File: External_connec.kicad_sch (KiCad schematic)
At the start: 8 parts, among them J2 A - B, J3 H - L, J4 TYPE-C-31-M12_13, J5 EXT_LOAD, J6 R4_TX, J7 R4_RX

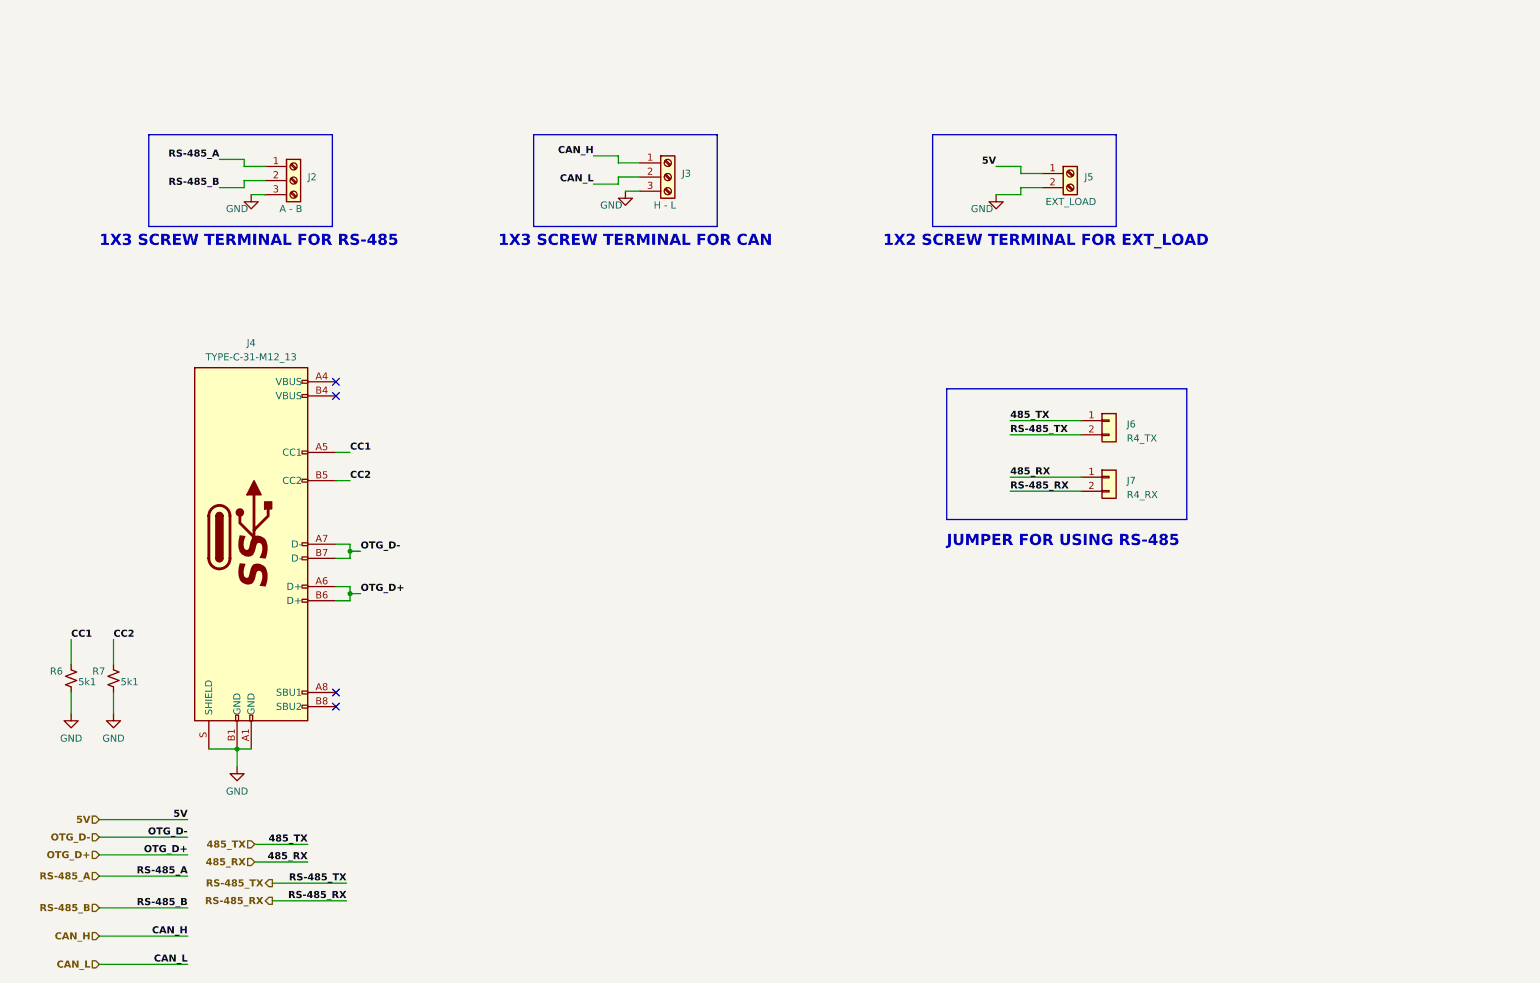
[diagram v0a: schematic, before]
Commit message: Added Female Headers
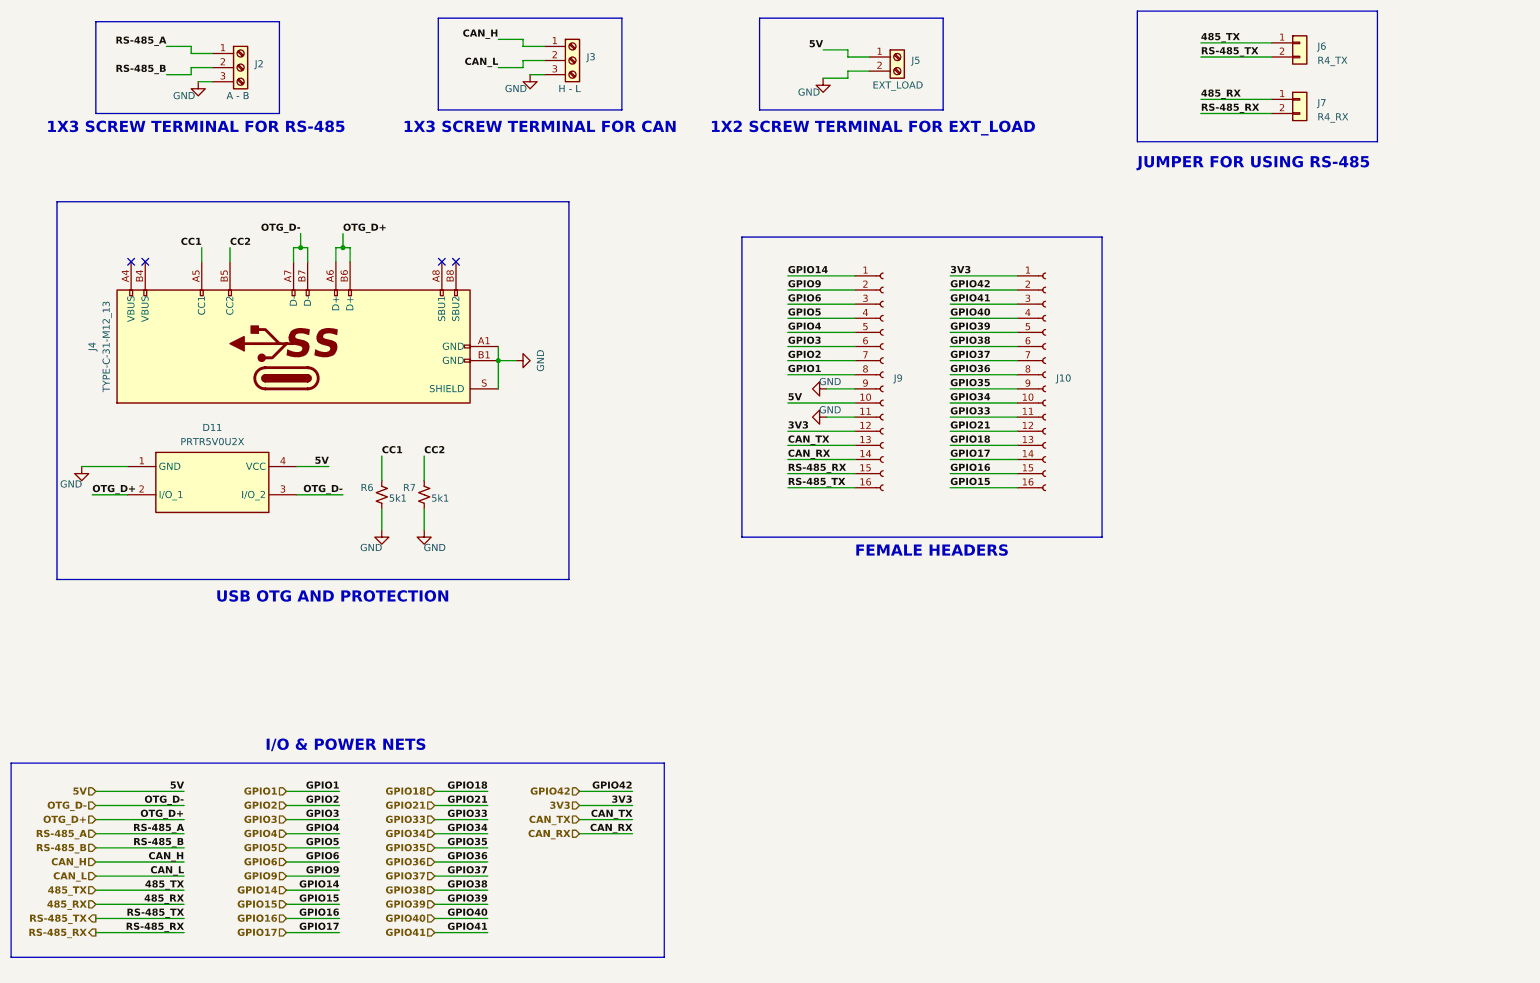
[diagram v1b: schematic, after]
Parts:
- added D11: PRTR5V0U2X, PRTR5V0U2X, symbol ESP32-S3_DB:PRTR5V0U2X
- added J10, J9: Conn_01x16_Socket, symbol ESP32-S3_DB:Conn_01x16_Socket
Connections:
- net 5V: now also D11.4 (VCC), J9.10 (Pin_10)
- net GND: now also D11.1 (GND), J9.11 (Pin_11), J9.9 (Pin_9)
- net OTG_D+: now also D11.2 (I/O_1)
- net OTG_D-: now also D11.3 (I/O_2)
- net RS-485_RX: now also J9.15 (Pin_15)
- net RS-485_TX: now also J9.16 (Pin_16)
- new net 3V3: J10.1 (Pin_1), J9.12 (Pin_12)
- new net CAN_RX: J9.14 (Pin_14)
- new net CAN_TX: J9.13 (Pin_13)
- new net GPIO1: J9.8 (Pin_8)
- new net GPIO14: J9.1 (Pin_1)
- new net GPIO15: J10.16 (Pin_16)
- new net GPIO16: J10.15 (Pin_15)
- new net GPIO17: J10.14 (Pin_14)
- new net GPIO18: J10.13 (Pin_13)
- new net GPIO2: J9.7 (Pin_7)
- new net GPIO21: J10.12 (Pin_12)
- new net GPIO3: J9.6 (Pin_6)
- new net GPIO33: J10.11 (Pin_11)
- new net GPIO34: J10.10 (Pin_10)
- new net GPIO35: J10.9 (Pin_9)
- new net GPIO36: J10.8 (Pin_8)
- new net GPIO37: J10.7 (Pin_7)
- new net GPIO38: J10.6 (Pin_6)
- new net GPIO39: J10.5 (Pin_5)
- new net GPIO4: J9.5 (Pin_5)
- new net GPIO40: J10.4 (Pin_4)
- new net GPIO41: J10.3 (Pin_3)
- new net GPIO42: J10.2 (Pin_2)
- new net GPIO5: J9.4 (Pin_4)
- new net GPIO6: J9.3 (Pin_3)
- new net GPIO9: J9.2 (Pin_2)
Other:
- note added: "FEMALE HEADERS"
- note added: "I/O & POWER NETS"
- note added: "USB OTG AND PROTECTION"
- moved on the sheet: J2, J3, J4, J5, J6, J7, R6, R7

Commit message: Completed header connections
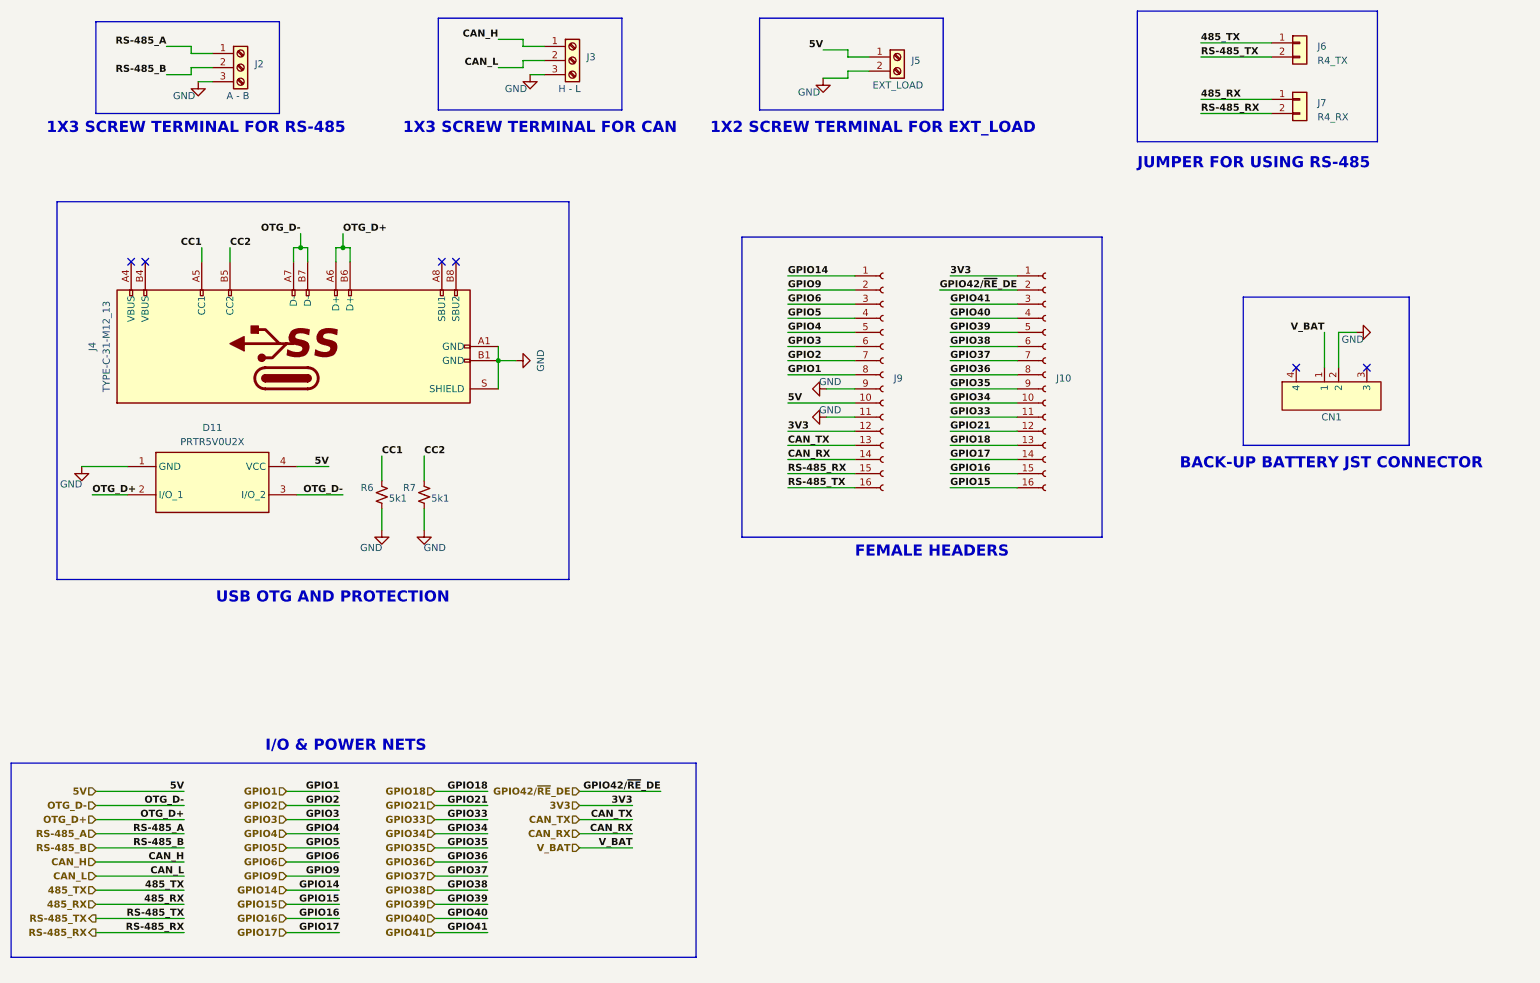
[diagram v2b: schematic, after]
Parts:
- added CN1: SM02B-SRSS-TB (LF)(SN), easyeda2kicad:CONN-SMD_2P-P1.00_SM02B-SRSS-TB-LF-SN, symbol ESP32-S3_DB:SM02B-SRSS-TB(LF)(SN)
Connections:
- net GND: now also CN1.2
- net GPIO42 renamed GPIO42/~{RE}_DE
- new net V_BAT: CN1.1
- no-connect marks 4 -> 6
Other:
- note added: "BACK-UP BATTERY JST CONNECTOR"
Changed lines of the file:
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@@
   (no_connect (at 93.98 66.675))
   (no_connect (at 35.56 66.675))
+  (no_connect (at 257.81 85.725))
   (no_connect (at 91.44 66.675))
+  (no_connect (at 245.11 85.725))
   (no_connect (at 38.1 66.675))
   (wire (pts (xy 73.025 187.325) (xy 63.5 187.325))
@@
     (stroke (width 0.5) (type default) (color 72 0 0 1))
   )
-  (bus (pts (xy 131.445 191.77) (xy 13.97 191.77))
+  (bus (pts (xy 137.16 191.77) (xy 13.97 191.77))
     (stroke (width 1) (type default) (color 72 72 72 1))
   )
@@
     (stroke (width 1) (type default) (color 72 72 72 1))
   )
+  (bus (pts (xy 235.585 73.025) (xy 235.585 99.695))
+    (stroke (width 1) (type default) (color 72 72 72 1))
+  )
   (wire (pts (xy 46.355 31.75) (xy 50.165 31.75))
     (stroke (width 0) (type default))
@@
     (stroke (width 0) (type default))
   )
-  (bus (pts (xy 13.97 156.845) (xy 131.445 156.845))
+  (bus (pts (xy 13.97 156.845) (xy 137.16 156.845))
     (stroke (width 1) (type default) (color 72 72 72 1))
   )
   (bus (pts (xy 216.535 21.59) (xy 216.535 45.085))
     (stroke (width 1) (type default) (color 72 72 72 1))
+  )
+  (wire (pts (xy 255.905 79.375) (xy 252.73 79.375))
+    (stroke (width 0) (type default))
   )
   (bus (pts (xy 123.825 39.37) (xy 90.805 39.37))
@@
     (stroke (width 0) (type default))
   )
+  (wire (pts (xy 125.73 172.085) (xy 116.205 172.085))
+    (stroke (width 0.5) (type default) (color 255 0 255 1))
+  )
   (wire (pts (xy 153.67 71.755) (xy 165.735 71.755))
     (stroke (width 0) (type default))
@@
     (stroke (width 0) (type default))
   )
+  (bus (pts (xy 265.43 73.025) (xy 265.43 99.695))
+    (stroke (width 1) (type default) (color 72 72 72 1))
+  )
   (wire (pts (xy 45.085 164.465) (xy 29.21 164.465))
     (stroke (width 0.5) (type default) (color 0 0 255 1))
@@
     (stroke (width 0.5) (type default) (color 72 0 0 1))
   )
+  (bus (pts (xy 265.43 99.695) (xy 235.585 99.695))
+    (stroke (width 1) (type default) (color 72 72 72 1))
+  )
   (wire (pts (xy 45.085 184.785) (xy 29.21 184.785))
     (stroke (width 0.5) (type default) (color 0 0 255 1))
@@
     (stroke (width 0) (type default))
   )
-  (wire (pts (xy 182.88 71.755) (xy 194.945 71.755))
+  (wire (pts (xy 180.975 71.755) (xy 194.945 71.755))
     (stroke (width 0) (type default))
   )
@@
     (stroke (width 1) (type default) (color 72 72 72 1))
   )
+  (wire (pts (xy 252.73 79.375) (xy 252.73 85.725))
+    (stroke (width 0) (type default))
+  )
   (bus (pts (xy 210.185 62.23) (xy 210.185 116.205))
     (stroke (width 1) (type default) (color 72 72 72 1))
@@
     (stroke (width 0) (type default))
   )
-  (bus (pts (xy 131.445 156.845) (xy 131.445 191.77))
+  (bus (pts (xy 137.16 156.845) (xy 137.16 191.77))
+    (stroke (width 1) (type default) (color 72 72 72 1))
+  )
+  (bus (pts (xy 235.585 73.025) (xy 265.43 73.025))
     (stroke (width 1) (type default) (color 72 72 72 1))
   )
@@
     (stroke (width 0) (type default))
   )
-  (wire (pts (xy 125.73 161.925) (xy 116.205 161.925))
+  (wire (pts (xy 130.81 161.925) (xy 116.205 161.925))
     (stroke (width 0.5) (type default) (color 72 0 0 1))
   )
@@
     (stroke (width 0) (type default))
   )
+  (wire (pts (xy 250.19 79.375) (xy 250.19 85.725))
+    (stroke (width 0) (type default))
+  )
   (wire (pts (xy 182.88 89.535) (xy 194.945 89.535))
     (stroke (width 0) (type default))
@@
     (effects (font (size 2 2) bold (color 0 0 255 1)) (justify left bottom))
   )
+  (text "BACK-UP BATTERY JST CONNECTOR" (at 224.155 104.14 0)
+    (effects (font (size 2 2) bold (color 255 0 0 1)) (justify left bottom))
+  )
   (label "GPIO40" (at 99.695 184.785 180) (fields_autoplaced)
     (effects (font (size 1.27 1.27) bold (color 72 0 0 1)) (justify right bottom))
@@
     (effects (font (size 1.27 1.27) bold (color 0 0 255 1)) (justify right bottom))
   )
+  (label "V_BAT" (at 250.19 79.375 180) (fields_autoplaced)
+    (effects (font (size 1.27 1.27) bold (color 255 0 255 1)) (justify right bottom))
+  )
   (label "GPIO34" (at 99.695 169.545 180) (fields_autoplaced)
     (effects (font (size 1.27 1.27) bold (color 72 0 0 1)) (justify right bottom))
@@
     (effects (font (size 1.27 1.27) bold (color 0 0 0 1)) (justify left bottom))
   )
-  (label "GPIO42" (at 182.88 71.755 0) (fields_autoplaced)
-    (effects (font (size 1.27 1.27) bold (color 72 0 0 1)) (justify left bottom))
-  )
   (label "5V" (at 160.02 28.575 180) (fields_autoplaced)
     (effects (font (size 1.27 1.27) bold (color 255 0 0 1)) (justify right bottom))
@@
     (effects (font (size 1.27 1.27) bold (color 0 0 0 1)) (justify right bottom))
   )
+  (label "V_BAT" (at 125.73 172.085 180) (fields_autoplaced)
+    (effects (font (size 1.27 1.27) bold (color 255 0 255 1)) (justify right bottom))
+  )
   (label "485_TX" (at 227.965 27.305 0) (fields_autoplaced)
     (effects (font (size 1.27 1.27) bold (color 0 0 255 1)) (justify left bottom))
@@
     (effects (font (size 1.27 1.27) bold (color 72 0 0 1)) (justify right bottom))
   )
+  (label "GPIO42{slash}~{RE}_DE" (at 180.975 71.755 0) (fields_autoplaced)
+    (effects (font (size 1.27 1.27) bold (color 72 0 0 1)) (justify left bottom))
+  )
   (label "GPIO38" (at 99.695 179.705 180) (fields_autoplaced)
     (effects (font (size 1.27 1.27) bold (color 72 0 0 1)) (justify right bottom))
   )
-  (label "GPIO42" (at 125.73 161.925 180) (fields_autoplaced)
+  (label "GPIO42{slash}~{RE}_DE" (at 130.81 161.925 180) (fields_autoplaced)
     (effects (font (size 1.27 1.27) bold (color 72 0 0 1)) (justify right bottom))
   )
@@
     (effects (font (size 1.27 1.27) (thickness 0.254) bold (color 72 0 72 1)) (justify right))
   )
-  (hierarchical_label "GPIO42" (shape input) (at 116.205 161.925 180) (fields_autoplaced)
+  (hierarchical_label "GPIO42{slash}~{RE}_DE" (shape input) (at 116.205 161.925 180) (fields_autoplaced)
     (effects (font (size 1.27 1.27) (thickness 0.254) bold (color 72 0 72 1)) (justify right))
   )
@@
   (hierarchical_label "GPIO18" (shape input) (at 90.17 161.925 180) (fields_autoplaced)
     (effects (font (size 1.27 1.27) (thickness 0.254) bold (color 72 0 72 1)) (justify right))
+  )
+  (hierarchical_label "V_BAT" (shape input) (at 116.205 172.085 180) (fields_autoplaced)
+    (effects (font (size 1.27 1.27) (thickness 0.254) bold (color 255 0 255 1)) (justify right))
   )
   (hierarchical_label "RS-485_B" (shape input) (at 29.21 172.085 180) (fields_autoplaced)
@@
     )
   )
+  (symbol (lib_id "ESP32-S3_DB:SM02B-SRSS-TB(LF)(SN)") (at 251.46 89.535 0) (unit 1)
+    (in_bom yes) (on_board yes) (dnp no)
+    (property "Reference" "CN1" (at 251.46 94.615 0)
+      (effects (font (size 1.27 1.27)))
+    )
+    (property "Value" "SM02B-SRSS-TB (LF)(SN)" (at 251.46 96.52 0)
+      (effects (font (size 1.27 1.27)) hide)
+    )
+    (property "Footprint" "easyeda2kicad:CONN-SMD_2P-P1.00_SM02B-SRSS-TB-LF-SN" (at 251.46 93.345 0)
+      (effects (font (size 1.27 1.27)) hide)
+    )
+    (property "Datasheet" "https://lcsc.com/product-detail/Others_JST-Sales-America__JST-Sales-America-SM02B-SRSS-TB-LF-SN_C160402.html" (at 251.46 95.885 0)
+      (effects (font (size 1.27 1.27)) hide)
+    )
+    (property "LCSC Part" "C160402" (at 251.46 98.425 0)
+      (effects (font (size 1.27 1.27)) hide)
+    )
+    (pin "1")
+    (pin "2")
+    (pin "3")
+    (pin "4")
+    (instances
+      (project "ESP32-S3_DB"
+        (path "/b7fc4bd3-c219-4455-832b-8d795385dcf1/e2721808-ce0b-4b73-8382-0fd911e1c931"
+          (reference "CN1") (unit 1)
+        )
+      )
+    )
+  )
   (symbol (lib_id "ESP32-S3_DB:GND") (at 26.67 103.505 0) (unit 1)
     (in_bom yes) (on_board yes) (dnp no)
@@
         )
       )
+    )
+  )
+  (symbol (lib_id "ESP32-S3_DB:GND") (at 255.905 79.375 90) (unit 1)
+    (in_bom yes) (on_board yes) (dnp no)
+    (property "Reference" "#PWR062" (at 262.255 79.375 0)
+      (effects (font (size 1.27 1.27)) hide)
+    )
+    (property "Value" "GND" (at 255.27 80.645 90)
+      (effects (font (size 1.27 1.27)))
+    )
+    (property "Footprint" "" (at 255.905 79.375 0)
+      (effects (font (size 1.27 1.27)) hide)
+    )
+    (property "Datasheet" "" (at 255.905 79.375 0)
+      (effects (font (size 1.27 1.27)) hide)
+    )
+    (pin "1")
+    (instances
+      (project "ESP32-S3_DB"
+        (path "/b7fc4bd3-c219-4455-832b-8d795385dcf1/e2721808-ce0b-4b73-8382-0fd911e1c931"
+          (reference "#PWR062") (unit 1)
+        )
+      )

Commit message: Assigned PN and Footprint for C
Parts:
- CN1: value SM02B-SRSS-TB (LF)(SN) -> JST_Battery; PN (none) -> SM02B-SRSS-TB (LF)(SN)
- D11: footprint PRTR5V0U2X -> (none)
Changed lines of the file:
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@@
       (effects (font (size 1.27 1.27)))
     )
-    (property "Footprint" "PRTR5V0U2X" (at 61.595 198.425 0)
+    (property "Footprint" "" (at 61.595 198.425 0)
       (effects (font (size 1.27 1.27)) (justify left top) hide)
     )
@@
       (effects (font (size 1.27 1.27)))
     )
-    (property "Value" "SM02B-SRSS-TB (LF)(SN)" (at 251.46 96.52 0)
+    (property "Value" "JST_Battery" (at 251.46 96.52 0)
       (effects (font (size 1.27 1.27)) hide)
     )
@@
       (effects (font (size 1.27 1.27)) hide)
     )
+    (property "PN" "SM02B-SRSS-TB (LF)(SN)" (at 251.46 89.535 0)
+      (effects (font (size 1.27 1.27)) hide)
+    )

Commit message: Assigned footprints
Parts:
- CN1: footprint easyeda2kicad:CONN-SMD_2P-P1.00_SM02B-SRSS-TB-LF-SN -> ESP32-S3_Dev_Board:CONN-SMD_2P-P1.00_SM02B-SRSS-TB-LF-SN
- D11: footprint (none) -> ESP32-S3_Dev_Board:SOT-143
- J4: footprint acheron_Connectors:TYPE-C-31-M-12 -> ESP32-S3_Dev_Board:USB-C_SMD-TYPE-C-31-M-12
- R6, R7: footprint (none) -> ESP32-S3_Dev_Board:R_0402_1005Metric; PN (none) -> RC0402FR-075K1L
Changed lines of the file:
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@@
       (effects (font (size 1.27 1.27)))
     )
-    (property "Footprint" "" (at 61.595 198.425 0)
+    (property "Footprint" "ESP32-S3_Dev_Board:SOT-143" (at 61.595 198.425 0)
       (effects (font (size 1.27 1.27)) (justify left top) hide)
     )
@@
       (effects (font (size 1.27 1.27)) (justify left))
     )
-    (property "Footprint" "" (at 80.645 108.585 0)
+    (property "Footprint" "ESP32-S3_Dev_Board:R_0402_1005Metric" (at 80.645 108.585 0)
       (effects (font (size 1.27 1.27)) hide)
     )
     (property "Datasheet" "~" (at 80.645 108.585 0)
+      (effects (font (size 1.27 1.27)) hide)
+    )
+    (property "PN" "RC0402FR-075K1L" (at 80.645 108.585 0)
       (effects (font (size 1.27 1.27)) hide)
     )
@@
       (effects (font (size 1.27 1.27)))
     )
-    (property "Footprint" "acheron_Connectors:TYPE-C-31-M-12" (at 63.5 94.615 90)
+    (property "Footprint" "ESP32-S3_Dev_Board:USB-C_SMD-TYPE-C-31-M-12" (at 63.5 94.615 90)
       (effects (font (size 1.27 1.27)) hide)
     )
@@
       (effects (font (size 1.27 1.27)) (justify left))
     )
-    (property "Footprint" "" (at 88.265 108.585 0)
+    (property "Footprint" "ESP32-S3_Dev_Board:R_0402_1005Metric" (at 88.265 108.585 0)
       (effects (font (size 1.27 1.27)) hide)
     )
@@
       (effects (font (size 1.27 1.27)) hide)
     )
+    (property "PN" "RC0402FR-075K1L" (at 88.265 108.585 0)
+      (effects (font (size 1.27 1.27)) hide)
+    )
     (pin "1")
     (pin "2")
@@
       (effects (font (size 1.27 1.27)) hide)
     )
-    (property "Footprint" "easyeda2kicad:CONN-SMD_2P-P1.00_SM02B-SRSS-TB-LF-SN" (at 251.46 93.345 0)
-      (effects (font (size 1.27 1.27)) hide)
-    )
+    (property "Footprint" "ESP32-S3_Dev_Board:CONN-SMD_2P-P1.00_SM02B-SRSS-TB-LF-SN" (at 251.46 93.345 0)
+      (effects (font (size 1.27 1.27)) hide)
+    )
